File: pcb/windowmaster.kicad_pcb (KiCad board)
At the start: 2 copper layers, 100 x 50 mm, 81 parts, among them J1 USB_C_Receptacle_USB2.0, J2 SWD, SW1 SW_DFU2, SW2 ENC, SW3 ENC, SW4 ENC, SW5 ENC, SW6 ENC, SW7 ENC, SW8 SW_DFU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

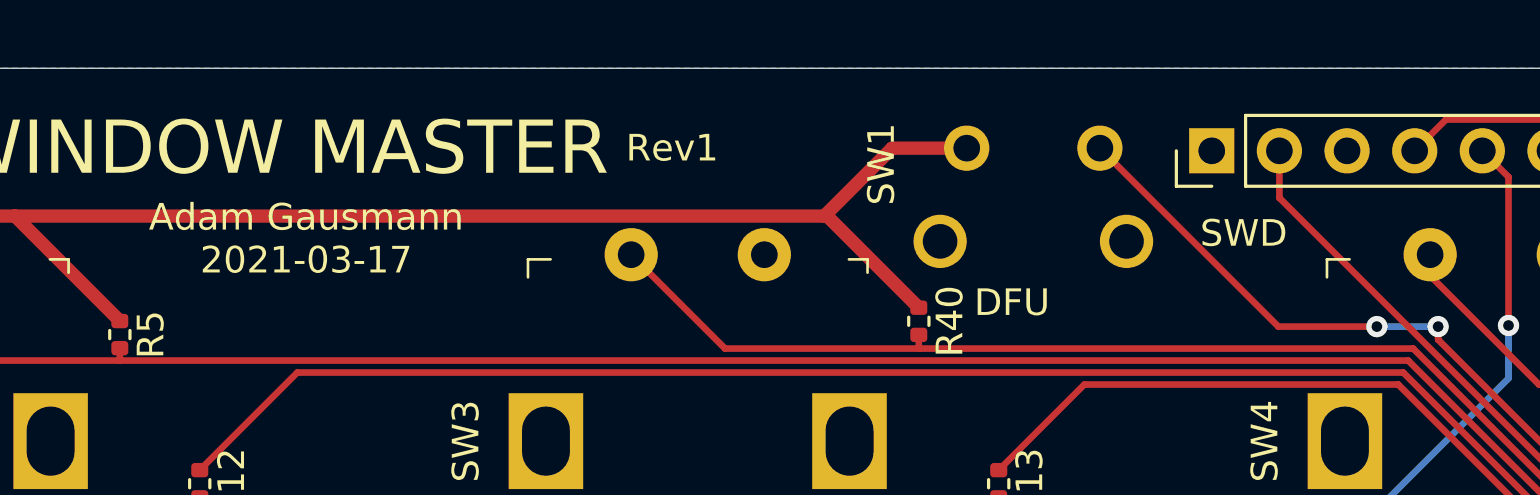
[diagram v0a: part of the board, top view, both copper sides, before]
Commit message: Fix MJTP1117 footprint
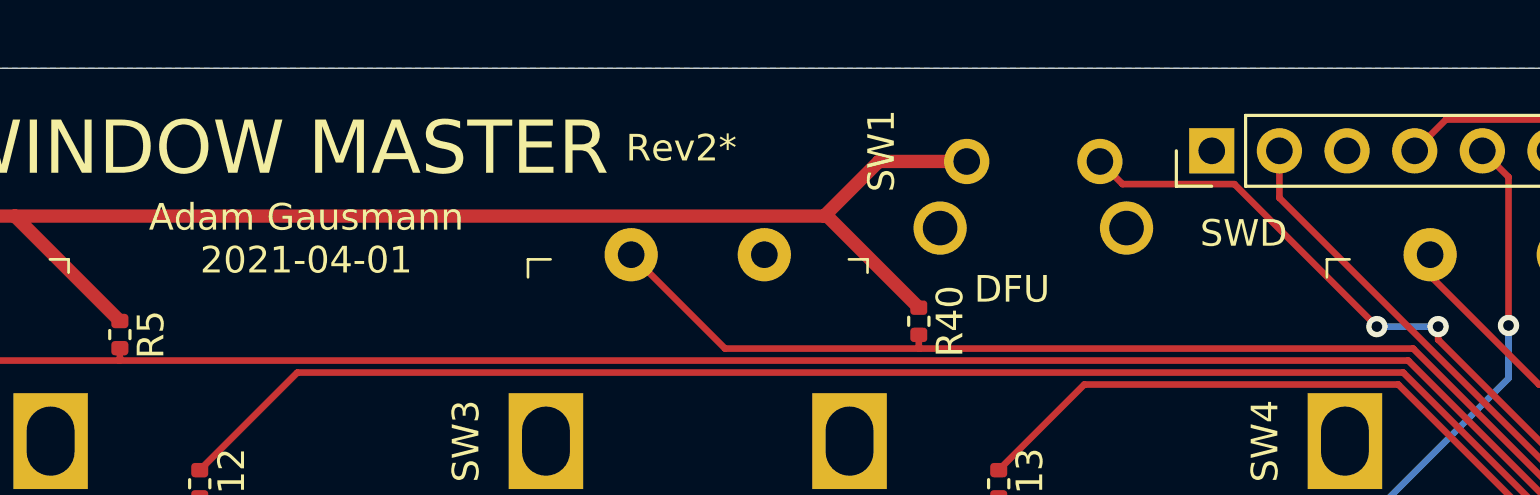
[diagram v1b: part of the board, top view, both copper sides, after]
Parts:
- moved SW1 0.50 mm to (195.3, 84.5)
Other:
- board text added: "Adam Gausmann 2021-04-01"
- board text added: "Rev2*"
- board text removed: "Adam Gausmann 2021-03-17"
- board text removed: "Rev1"
